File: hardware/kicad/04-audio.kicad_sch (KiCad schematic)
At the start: 9 parts, among them U5 PAM8403

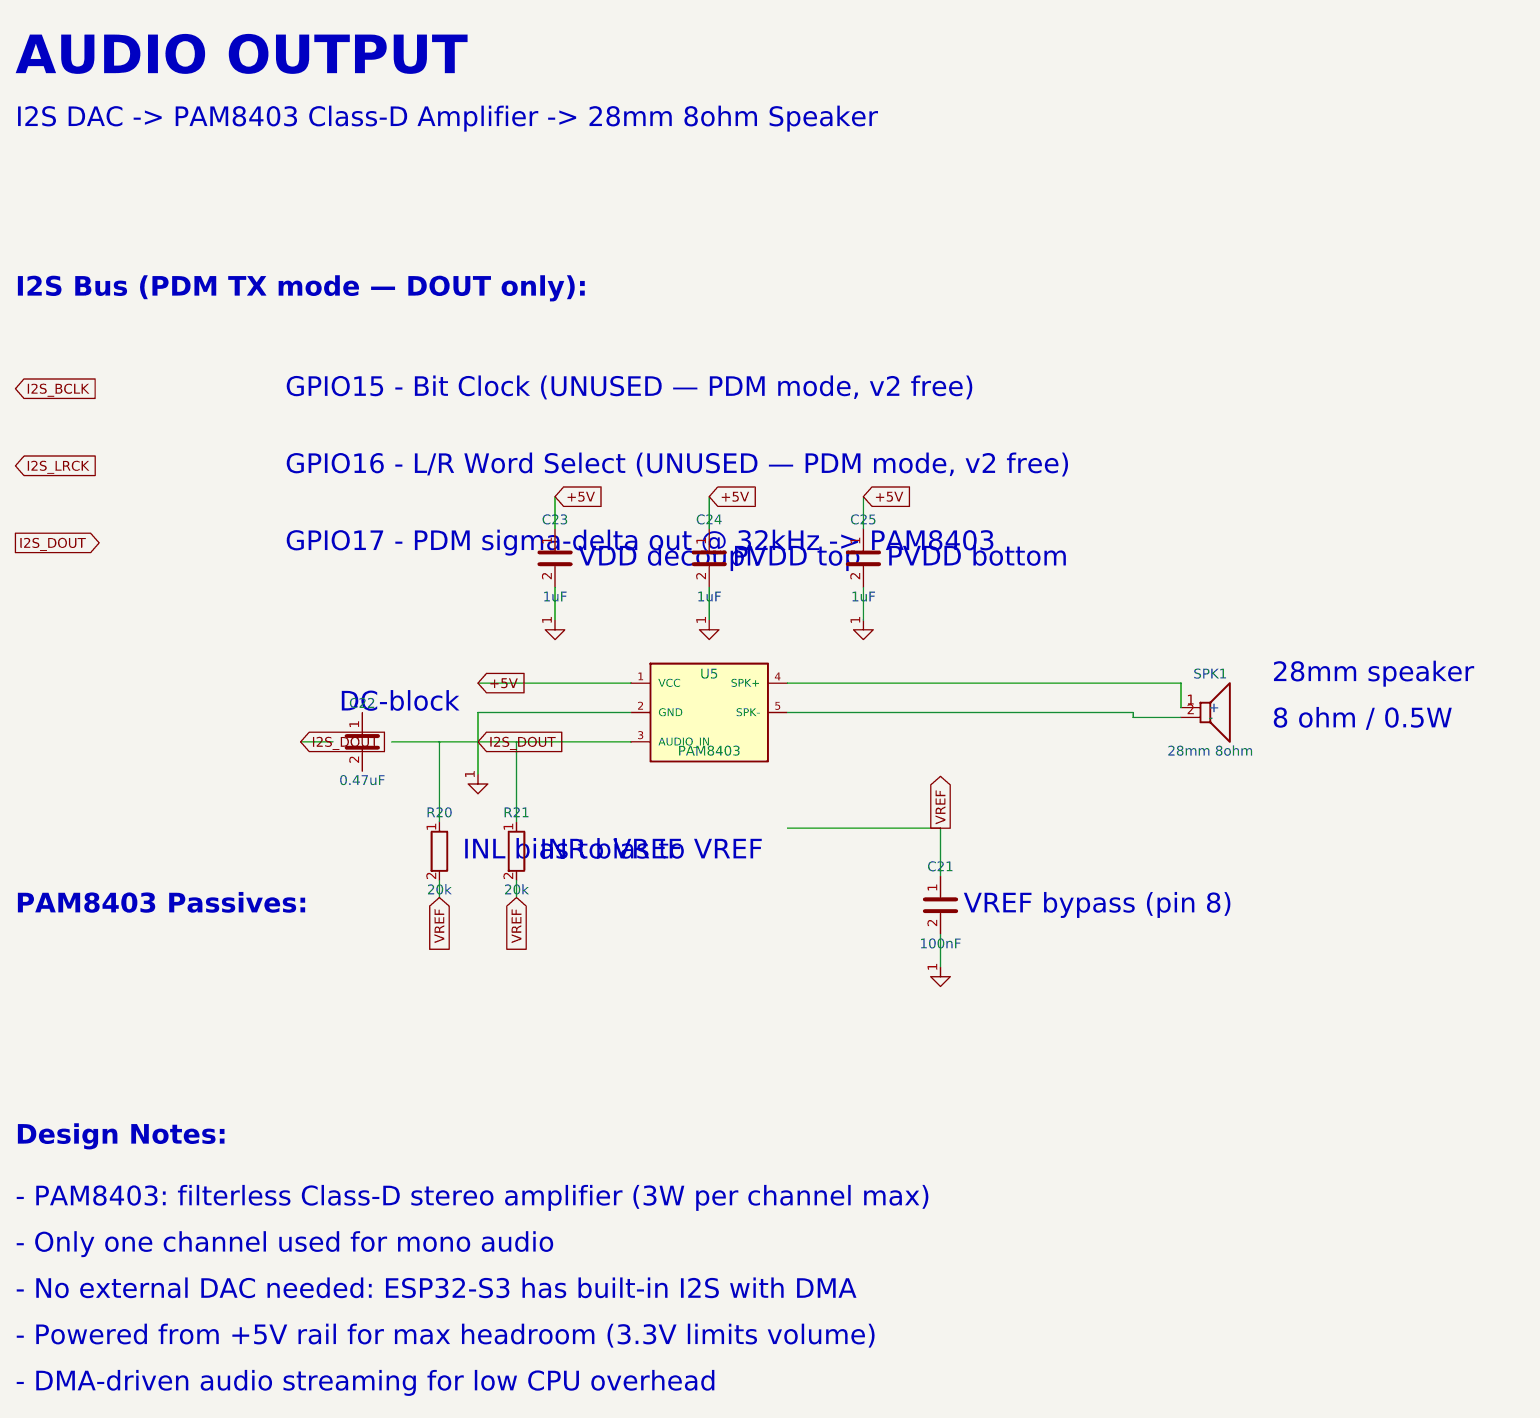
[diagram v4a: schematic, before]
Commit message: sch(layout): fix annotation overlaps across all 6 sheets — reflow to A3 where needed
Root cause: multiple sheets had annotation text boxes placed too close
to each other or to component symbols/net labels. On the live website
this rendered as strings running through each other and through
component pins — unreadable in the schematic viewer.

Per-sheet fixes:

* Sheet 1 — Power Supply
  - Upgraded to A3 landscape (was A4). USB ESD (U4/R22/R23) had
    been placed at (45, 160) directly on top of SW_PWR, C1, U3
    and C2 — all at y=160. There was no room on A4 to fit both
    the input stage (USB-C + IP5306 + battery) and the output
    stage (AMS1117 + LEDs + power switch + USB ESD) with clean
    annotations.
  - USB ESD block relocated to its own dedicated row (y=140).
  - CHARGING INDICATOR LEDs moved to a dedicated right-side zone
    (x=275, y=145) so they no longer collide with USB ESD.
  - POWER SWITCH moved to its own right-side zone (x=285, y=200)
    so its long "v1 as-built" help text no longer crosses through
    C1 / U3 (AMS1117) / C2.
  - VOLTAGE REGULATOR title + AMS1117 area pushed down (y=175 /
    y=200) with DESIGN NOTES following (y=240).
  - C18 (BAT bypass) moved left of Q1, out of the "P-MOSFET RPP /
    SI2301CDS" label zone; C27 (HF bypass) spaced further from C19
    (was 15mm gap, now 22mm) so "VOUT bulk" label no longer runs
    into "HF bypass".
  - Q1 dual annotation stacked with 3mm vertical spacing (was 2mm).
  - R24 label moved BELOW its symbol as "Q1 gate PD".
  - J3 / BT1 pushed further right (jst_x=268, bt_x=315) to use A3
    width and clear the Q1 cluster.

* Sheet 2 — MCU (ESP32-S3)
  - EN pull-up annotation shortened + moved up so it no longer
    collides with the "RC reset delay" label below.
  - BOOT switch pushed further down (c_en_y + 55) and left of the
    RESET switch so its BTN_SELECT glabel and help text no longer
    overlap the DISPLAY / AUDIO / CONTROLS annotation column. Help
    text now sits below the switch in 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
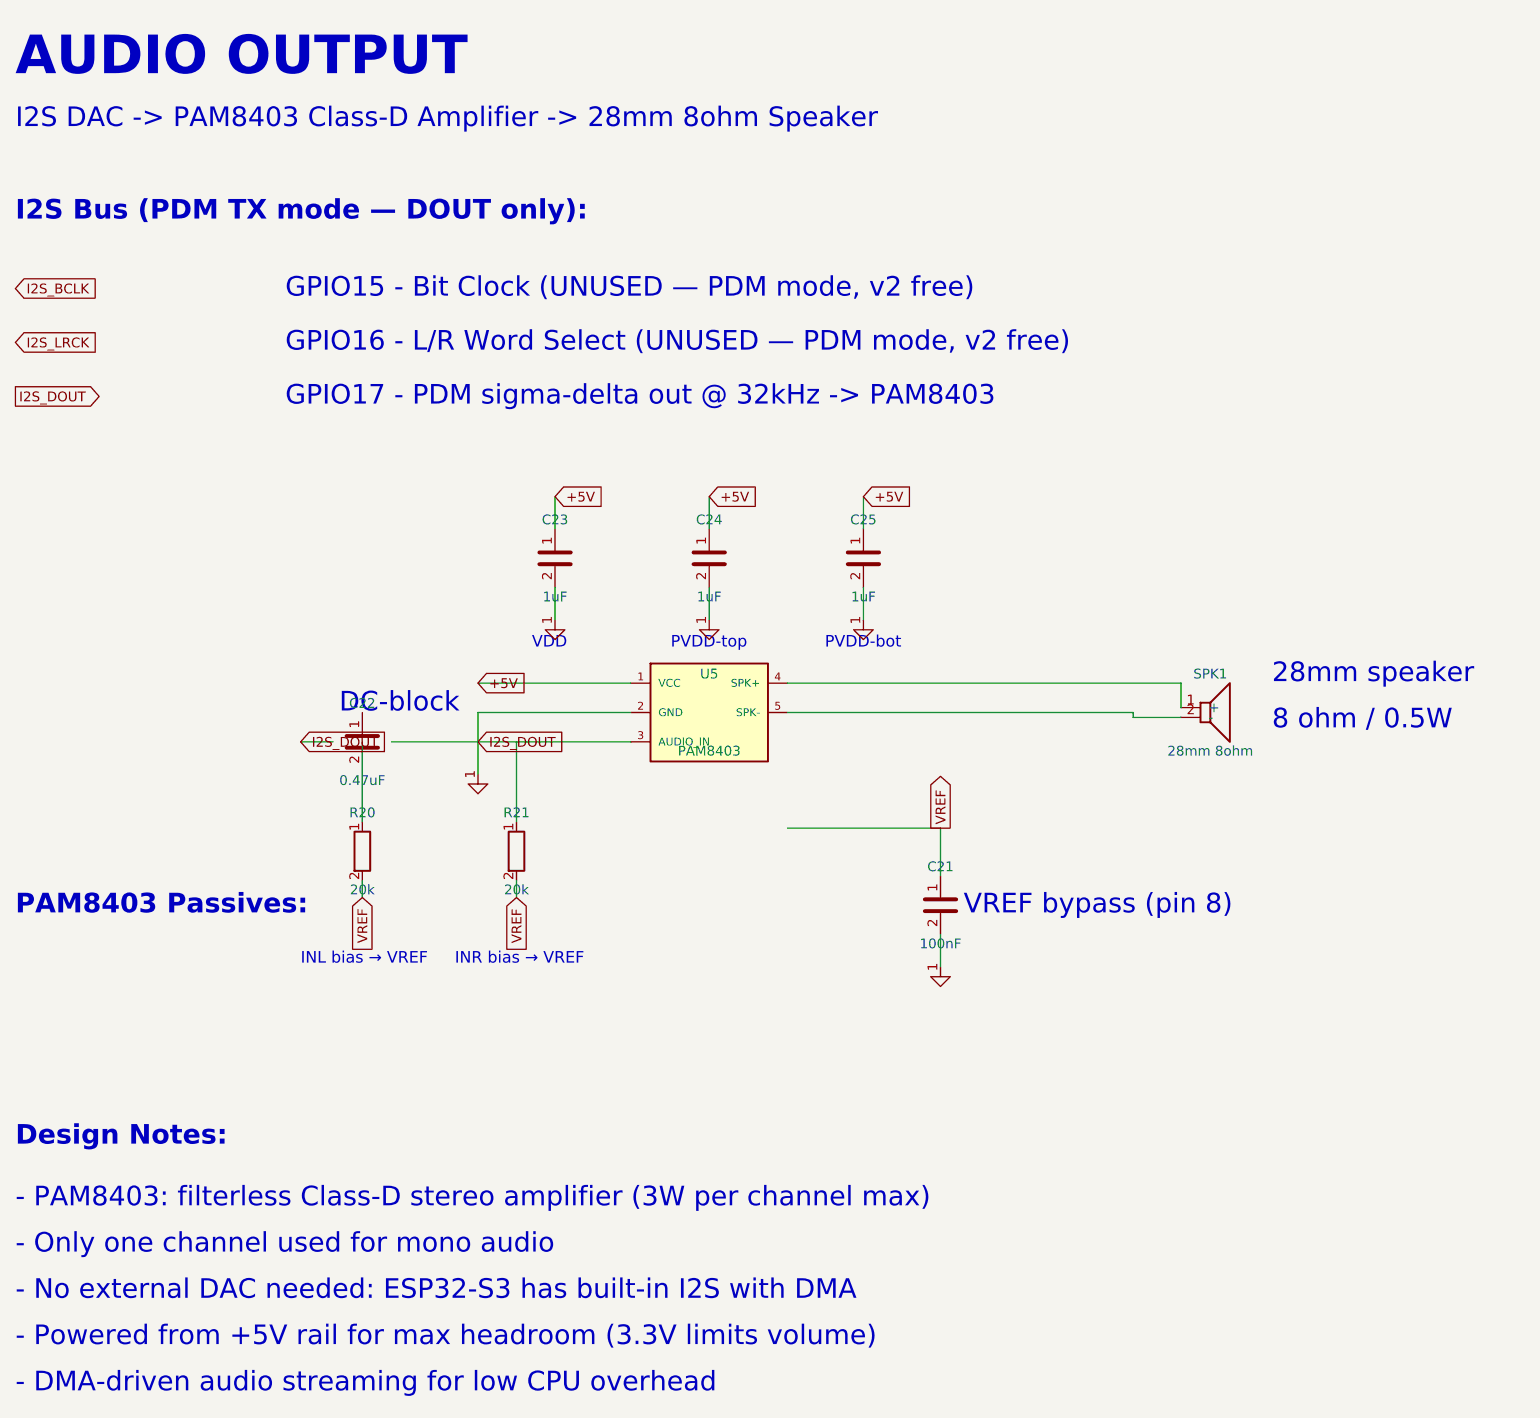
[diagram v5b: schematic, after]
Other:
- note added: "INL bias → VREF"
- note added: "INR bias → VREF"
- note added: "PVDD-bot"
- note added: "PVDD-top"
- note added: "VDD"
- note removed: "INL bias to VREF"
- note removed: "INR bias to VREF"
- note removed: "PVDD bottom"
- note removed: "PVDD top"
- note removed: "VDD decoupl."
- moved on the sheet: R20
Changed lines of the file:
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@@
   (global_label "I2S_DOUT" (shape input) (at 90 113.81 0) (effects (font (size 1.27 1.27))) (property "Intersheetrefs" "" (at 0 0 0) (effects (font (size 1.27 1.27)) hide)))
   (wire (pts (xy 90 113.81) (xy 109.84 113.81)) (stroke (width 0) (type default)))
-  (text "I2S Bus (PDM TX mode — DOUT only):" (at 30 55 0) (effects (font (size 2.54 2.54) bold) (justify left)))
-  (global_label "I2S_BCLK" (shape input) (at 30 68 0) (effects (font (size 1.27 1.27))) (property "Intersheetrefs" "" (at 0 0 0) (effects (font (size 1.27 1.27)) hide)))
-  (text "GPIO15 - Bit Clock (UNUSED — PDM mode, v2 free)" (at 65 68 0) (effects (font (size 2.54 2.54)) (justify left)))
-  (global_label "I2S_LRCK" (shape input) (at 30 78 0) (effects (font (size 1.27 1.27))) (property "Intersheetrefs" "" (at 0 0 0) (effects (font (size 1.27 1.27)) hide)))
-  (text "GPIO16 - L/R Word Select (UNUSED — PDM mode, v2 free)" (at 65 78 0) (effects (font (size 2.54 2.54)) (justify left)))
-  (global_label "I2S_DOUT" (shape output) (at 30 88 0) (effects (font (size 1.27 1.27))) (property "Intersheetrefs" "" (at 0 0 0) (effects (font (size 1.27 1.27)) hide)))
-  (text "GPIO17 - PDM sigma-delta out @ 32kHz -> PAM8403" (at 65 88 0) (effects (font (size 2.54 2.54)) (justify left)))
+  (text "I2S Bus (PDM TX mode — DOUT only):" (at 30 45 0) (effects (font (size 2.54 2.54) bold) (justify left)))
+  (global_label "I2S_BCLK" (shape input) (at 30 55 0) (effects (font (size 1.27 1.27))) (property "Intersheetrefs" "" (at 0 0 0) (effects (font (size 1.27 1.27)) hide)))
+  (text "GPIO15 - Bit Clock (UNUSED — PDM mode, v2 free)" (at 65 55 0) (effects (font (size 2.54 2.54)) (justify left)))
+  (global_label "I2S_LRCK" (shape input) (at 30 62 0) (effects (font (size 1.27 1.27))) (property "Intersheetrefs" "" (at 0 0 0) (effects (font (size 1.27 1.27)) hide)))
+  (text "GPIO16 - L/R Word Select (UNUSED — PDM mode, v2 free)" (at 65 62 0) (effects (font (size 2.54 2.54)) (justify left)))
+  (global_label "I2S_DOUT" (shape output) (at 30 69 0) (effects (font (size 1.27 1.27))) (property "Intersheetrefs" "" (at 0 0 0) (effects (font (size 1.27 1.27)) hide)))
+  (text "GPIO17 - PDM sigma-delta out @ 32kHz -> PAM8403" (at 65 69 0) (effects (font (size 2.54 2.54)) (justify left)))
   (symbol (lib_id "Speaker") (at 185 110 0) (unit 1) (exclude_from_sim no) (in_bom yes) (on_board yes) (dnp no) (property "Reference" "SPK1" (at 185 105 0) (effects (font (size 1.27 1.27)))) (property "Value" "28mm 8ohm" (at 185 115 0) (effects (font (size 1.27 1.27)))) (pin "1") (pin "2"))
   (text "28mm speaker" (at 193 105 0) (effects (font (size 2.54 2.54)) (justify left)))
@@
   (global_label "I2S_DOUT" (shape input) (at 67 113.81 0) (effects (font (size 1.27 1.27))) (property "Intersheetrefs" "" (at 0 0 0) (effects (font (size 1.27 1.27)) hide)))
   (text "DC-block" (at 72 108.81 0) (effects (font (size 2.54 2.54)) (justify left)))
-  (symbol (lib_id "R") (at 85 128 0) (unit 1) (exclude_from_sim no) (in_bom yes) (on_board yes) (dnp no) (property "Reference" "R20" (at 85 123 0) (effects (font (size 1.27 1.27)))) (property "Value" "20k" (at 85 133 0) (effects (font (size 1.27 1.27)))) (pin "1") (pin "2"))
-  (wire (pts (xy 85 124.19) (xy 85 113.81)) (stroke (width 0) (type default)))
-  (wire (pts (xy 85 131.81) (xy 85 134)) (stroke (width 0) (type default)))
-  (global_label "VREF" (shape input) (at 85 134 270) (effects (font (size 1.27 1.27))) (property "Intersheetrefs" "" (at 0 0 0) (effects (font (size 1.27 1.27)) hide)))
-  (text "INL bias to VREF" (at 88 128 0) (effects (font (size 2.54 2.54)) (justify left)))
+  (symbol (lib_id "R") (at 75 128 0) (unit 1) (exclude_from_sim no) (in_bom yes) (on_board yes) (dnp no) (property "Reference" "R20" (at 75 123 0) (effects (font (size 1.27 1.27)))) (property "Value" "20k" (at 75 133 0) (effects (font (size 1.27 1.27)))) (pin "1") (pin "2"))
+  (wire (pts (xy 75 124.19) (xy 75 113.81)) (stroke (width 0) (type default)))
+  (wire (pts (xy 75 131.81) (xy 75 134)) (stroke (width 0) (type default)))
+  (global_label "VREF" (shape input) (at 75 134 270) (effects (font (size 1.27 1.27))) (property "Intersheetrefs" "" (at 0 0 0) (effects (font (size 1.27 1.27)) hide)))
+  (text "INL bias → VREF" (at 67 142 0) (effects (font (size 1.5 1.5)) (justify left)))
   (symbol (lib_id "R") (at 95 128 0) (unit 1) (exclude_from_sim no) (in_bom yes) (on_board yes) (dnp no) (property "Reference" "R21" (at 95 123 0) (effects (font (size 1.27 1.27)))) (property "Value" "20k" (at 95 133 0) (effects (font (size 1.27 1.27)))) (pin "1") (pin "2"))
   (wire (pts (xy 95 124.19) (xy 95 113.81)) (stroke (width 0) (type default)))
   (wire (pts (xy 95 131.81) (xy 95 134)) (stroke (width 0) (type default)))
   (global_label "VREF" (shape input) (at 95 134 270) (effects (font (size 1.27 1.27))) (property "Intersheetrefs" "" (at 0 0 0) (effects (font (size 1.27 1.27)) hide)))
-  (text "INR bias to VREF" (at 98 128 0) (effects (font (size 2.54 2.54)) (justify left)))
+  (text "INR bias → VREF" (at 87 142 0) (effects (font (size 1.5 1.5)) (justify left)))
   (symbol (lib_id "C") (at 100 90 0) (unit 1) (exclude_from_sim no) (in_bom yes) (on_board yes) (dnp no) (property "Reference" "C23" (at 100 85 0) (effects (font (size 1.27 1.27)))) (property "Value" "1uF" (at 100 95 0) (effects (font (size 1.27 1.27)))) (pin "1") (pin "2"))
   (global_label "+5V" (shape input) (at 100 82 0) (effects (font (size 1.27 1.27))) (property "Intersheetrefs" "" (at 0 0 0) (effects (font (size 1.27 1.27)) hide)))
@@
   (symbol (lib_id "GND") (at 100 98 0) (unit 1) (exclude_from_sim no) (in_bom no) (on_board no) (dnp no) (property "Reference" "#PWR003" (at 100 96 0) (effects (font (size 1.27 1.27)) hide)) (property "Value" "GND" (at 100 100 0) (effects (font (size 1.27 1.27)) hide)) (pin "1"))
   (wire (pts (xy 100 93.81) (xy 100 98)) (stroke (width 0) (type default)))
-  (text "VDD decoupl." (at 103 90 0) (effects (font (size 2.54 2.54)) (justify left)))
+  (text "VDD" (at 97 101 0) (effects (font (size 1.5 1.5)) (justify left)))
   (symbol (lib_id "C") (at 120 90 0) (unit 1) (exclude_from_sim no) (in_bom yes) (on_board yes) (dnp no) (property "Reference" "C24" (at 120 85 0) (effects (font (size 1.27 1.27)))) (property "Value" "1uF" (at 120 95 0) (effects (font (size 1.27 1.27)))) (pin "1") (pin "2"))
   (global_label "+5V" (shape input) (at 120 82 0) (effects (font (size 1.27 1.27))) (property "Intersheetrefs" "" (at 0 0 0) (effects (font (size 1.27 1.27)) hide)))
@@
   (symbol (lib_id "GND") (at 120 98 0) (unit 1) (exclude_from_sim no) (in_bom no) (on_board no) (dnp no) (property "Reference" "#PWR004" (at 120 96 0) (effects (font (size 1.27 1.27)) hide)) (property "Value" "GND" (at 120 100 0) (effects (font (size 1.27 1.27)) hide)) (pin "1"))
   (wire (pts (xy 120 93.81) (xy 120 98)) (stroke (width 0) (type default)))
-  (text "PVDD top" (at 123 90 0) (effects (font (size 2.54 2.54)) (justify left)))
+  (text "PVDD-top" (at 115 101 0) (effects (font (size 1.5 1.5)) (justify left)))
   (symbol (lib_id "C") (at 140 90 0) (unit 1) (exclude_from_sim no) (in_bom yes) (on_board yes) (dnp no) (property "Reference" "C25" (at 140 85 0) (effects (font (size 1.27 1.27)))) (property "Value" "1uF" (at 140 95 0) (effects (font (size 1.27 1.27)))) (pin "1") (pin "2"))
   (global_label "+5V" (shape input) (at 140 82 0) (effects (font (size 1.27 1.27))) (property "Intersheetrefs" "" (at 0 0 0) (effects (font (size 1.27 1.27)) hide)))
@@
   (symbol (lib_id "GND") (at 140 98 0) (unit 1) (exclude_from_sim no) (in_bom no) (on_board no) (dnp no) (property "Reference" "#PWR005" (at 140 96 0) (effects (font (size 1.27 1.27)) hide)) (property "Value" "GND" (at 140 100 0) (effects (font (size 1.27 1.27)) hide)) (pin "1"))
   (wire (pts (xy 140 93.81) (xy 140 98)) (stroke (width 0) (type default)))
-  (text "PVDD bottom" (at 143 90 0) (effects (font (size 2.54 2.54)) (justify left)))
+  (text "PVDD-bot" (at 135 101 0) (effects (font (size 1.5 1.5)) (justify left)))
   (text "Design Notes:" (at 30 165 0) (effects (font (size 2.54 2.54) bold) (justify left)))
   (text "- PAM8403: filterless Class-D stereo amplifier (3W per channel max)" (at 30 173 0) (effects (font (size 2.54 2.54)) (justify left)))
